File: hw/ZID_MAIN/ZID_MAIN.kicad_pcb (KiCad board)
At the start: 6 copper layers, 127 x 88.9 mm, 181 parts, among them J1 Conn 1x04 0.1" Socket, J10 FFC/FPC-40 Socket, J11 JST-PH-K B6B, J14 USB-C PWR ONLY, J15 Conn 2x03 pin hdr 0.1", J2 JST-PH-K B6B, J3 Conn 1x02 0.1" pin, J4 Conn 1x03 0.1" pin, J5 Conn 1x08 0.1" pin, J6 Conn 1x08 0.1" pin, J7 Conn 2x04 0.1" pin, J8 Conn 2x02 0.1" pin, J9 Conn 2x04 0.1" pin, M1 WS-RP2040-Zero, SW1 SW_Push, SW2 SW_DIP_x02, U1 OSC-20MHz, U10 27WZ06, U11 74LVC125AS, U12 74LVC273, U13 74FCT2245, U14 AS7C1024B, U15 ATF1508AS, U16 74FCT2245, U17 74HCT166, U18 ATF1508AS, U19 74HCT166, U2 74FCT2245, U20 74FCT2244, U22 ATF1504AS-44T, U23 74AHCT00, U24 74FCT2244, U3 24LC32, U4 MIC2775, U5 SST39SF010, U6 74LVC245, U7 74FCT2245, U8 74AHCT14, U9 Z80 C20MHz-PLCC

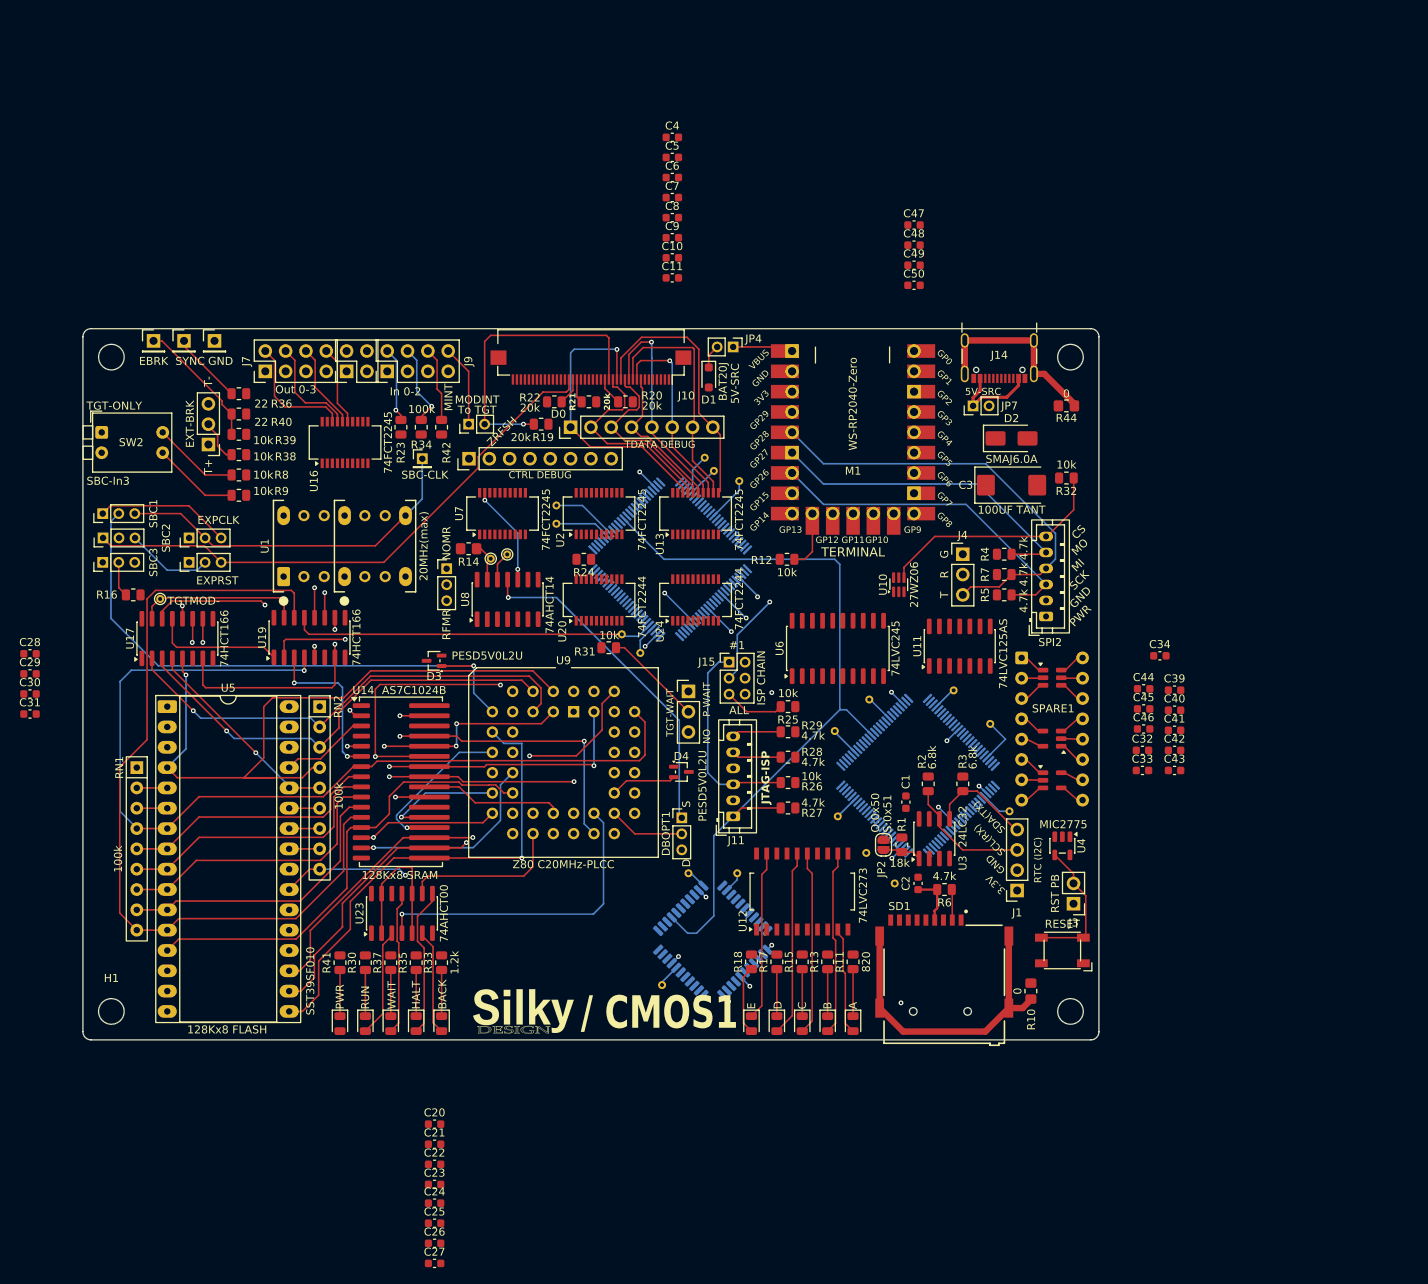
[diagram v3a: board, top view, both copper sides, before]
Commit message: PCB: Save before 'rip-out' (3.5x5.0)
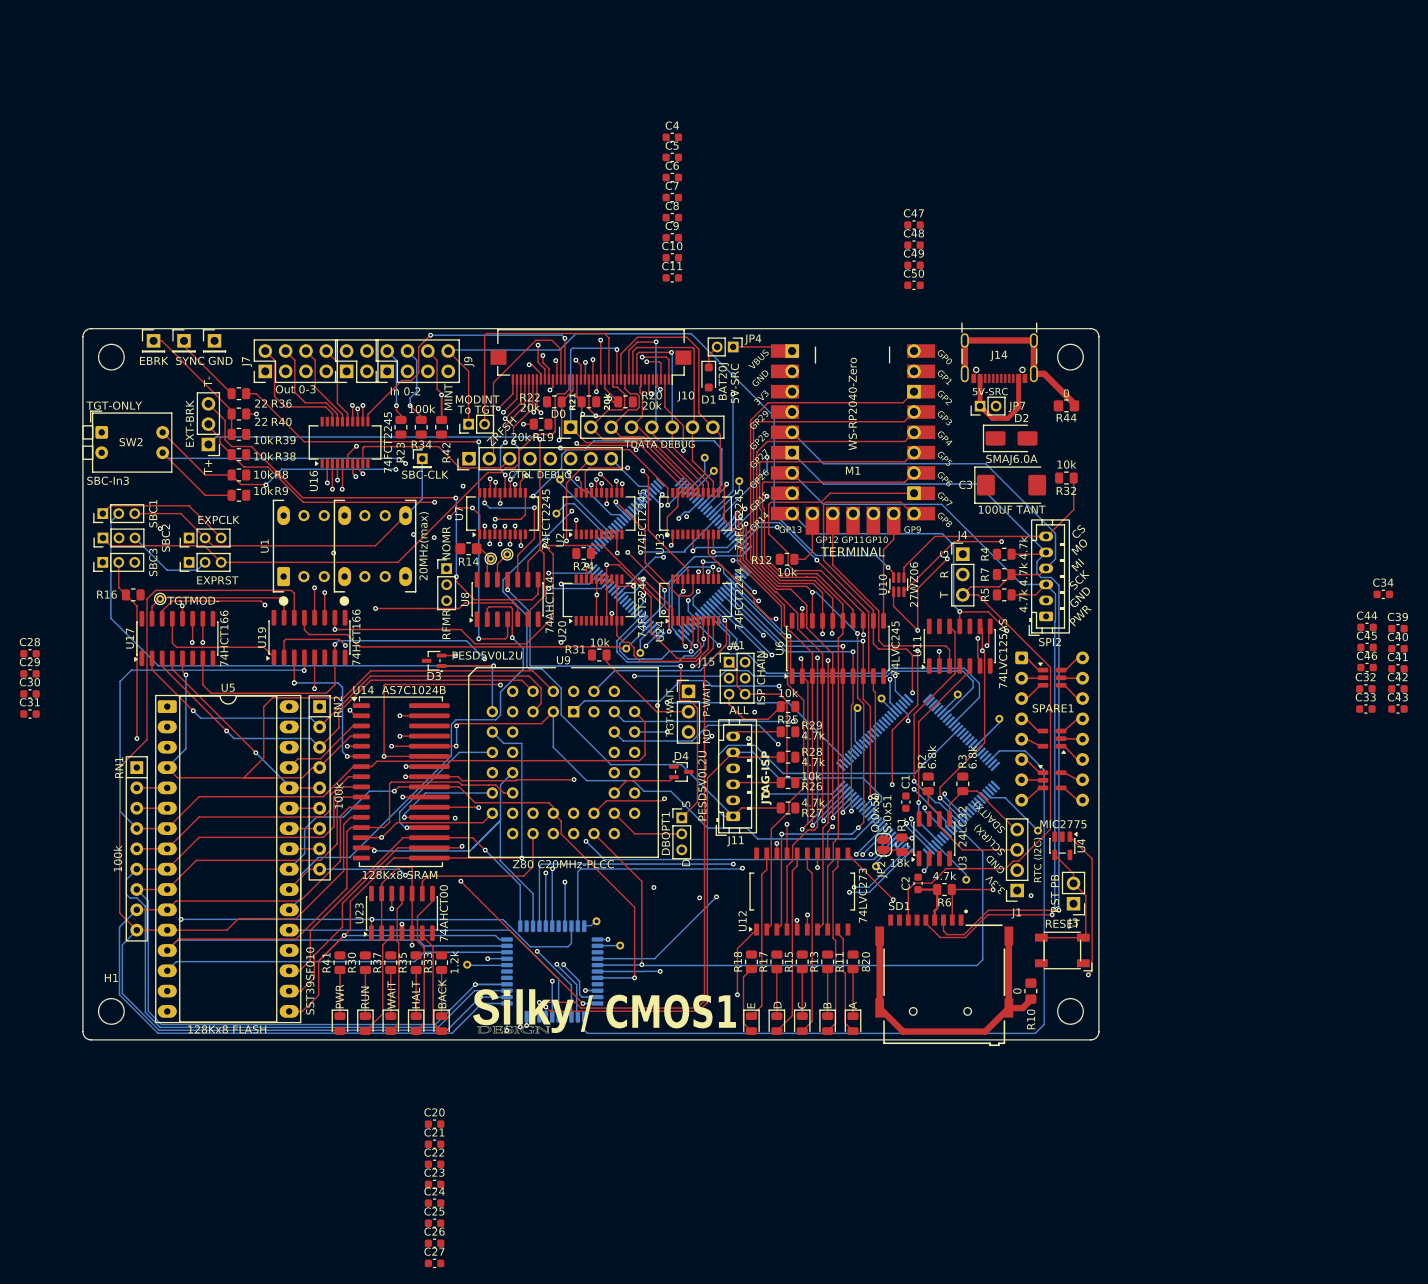
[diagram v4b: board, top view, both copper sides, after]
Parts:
- moved C32 29.0 mm to (219.1, 100.9)
- moved C33 29.0 mm to (219.1, 103.4)
- moved C34 29.0 mm to (221.3, 89.1)
- moved C39 29.0 mm to (223.1, 93.4)
- moved C40 29.0 mm to (223.1, 95.9)
- moved C41 29.0 mm to (223.1, 98.4)
- moved C42 29.0 mm to (223.1, 100.9)
- moved C43 29.0 mm to (223.1, 103.4)
- moved C44 29.0 mm to (219.3, 93.2)
- moved C45 29.0 mm to (219.3, 95.7)
- moved C46 29.0 mm to (219.3, 98.2)
- moved TP22 24.5 mm to (106.8, 135.4), turned to 180 degrees
- moved TP19 22.4 mm to (155.6, 103.3)
- moved TP18 20.5 mm to (178.1, 118.6)
- moved U22 20.5 mm to (117.4, 136.2), turned to 90 degrees
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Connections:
- U2 pad 11: /TA0 -> /TA2
- U2 pad 13: /TA2 -> /TA0
- U2 pad 14: /TA3 -> /TA15
- U2 pad 15: /TA4 -> /TA14
- U2 pad 16: /TA5 -> /TA13
- U2 pad 17: /TA6 -> /TA12
- U2 pad 18: /TA7 -> /TA11
- U2 pad 2: /ZA7 -> /ZA11
- U2 pad 3: /ZA6 -> /ZA12
- U2 pad 4: /ZA5 -> /ZA13
- U2 pad 5: /ZA4 -> /ZA14
- U2 pad 6: /ZA3 -> /ZA15
- U2 pad 7: /ZA2 -> /ZA0
- U2 pad 9: /ZA0 -> /ZA2
- U7 pad 11: /TA8 -> /TA3
- U7 pad 12: /TA9 -> /TA4
- U7 pad 13: /TA10 -> /TA5
- U7 pad 14: /TA11 -> /TA6
- U7 pad 15: /TA12 -> /TA7
- U7 pad 16: /TA13 -> /TA8
- U7 pad 17: /TA14 -> /TA9
- U7 pad 18: /TA15 -> /TA10
- U7 pad 2: /ZA15 -> /ZA10
- U7 pad 3: /ZA14 -> /ZA9
- U7 pad 4: /ZA13 -> /ZA8
- U7 pad 5: /ZA12 -> /ZA7
- U7 pad 6: /ZA11 -> /ZA6
- U7 pad 7: /ZA10 -> /ZA5
- U7 pad 8: /ZA9 -> /ZA4
- U7 pad 9: /ZA8 -> /ZA3
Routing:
- net /ZRD-: track 17.3 -> 233.7 mm, vias 0 -> 6
- net /ZWR-: track 49.7 -> 264.3 mm, vias 2 -> 7
- net /RST-: track 10.8 -> 211.3 mm, vias 0 -> 1
- net /TGTMODE-: track 20.9 -> 220.7 mm, vias 0 -> 4
- net /LRST-: track 19.0 -> 203.6 mm, vias 0 -> 4
- net /ZA0: track 103.1 -> 269.1 mm, vias 0 -> 2
- net /ZD1: track 57.7 -> 221.8 mm, vias 1 -> 3
- net /ZA3: track 160.1 -> 313.1 mm, vias 1 -> 6
- net /ZD0: track 57.9 -> 210.8 mm, vias 0 -> 3
- net /ZM1-: track 0.00 -> 136.5 mm, vias 0 -> 1
- net /TWAIT-: track 3.04 -> 134.7 mm, vias 0 -> 3
- net /ZBACK-: track 39.9 -> 165.6 mm, vias 1 -> 8
- net /MRST-: track 0.00 -> 119.3 mm, vias 0 -> 3
- net /ZRFSH-: track 8.27 -> 121.6 mm, vias 0 -> 1
- net /ZD6: track 43.8 -> 152.2 mm, vias 1 -> 5
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
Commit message: PCB: Checkpoint... 349 nets left
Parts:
- added U21: 74LVC2G34, Package_TO_SOT_SMD:SOT-23-6, F.Cu at (163.9, 82.5)
- R12, R16, R24, R31, R38, R39, R8, R9: value 10k -> 20k
- U10: value 27WZ06 -> 74LVC2G06
- U11: value 74LVC125AS -> 74LVC2G34; footprint Package_SO:SOIC-14_3.9x8.7mm_P1.27mm -> Package_TO_SOT_SMD:SOT-23-6
- U3: value 24LC32 -> 24LC32A EEP
- moved SPARE1 92.8 mm to (87.9, 126.0), turned to 90 degrees
- moved TP10 62.3 mm to (179.4, 87.1)
- moved TP11 60.0 mm to (177.4, 87.0)
- moved TP5 56.6 mm to (183.5, 103.6)
- moved TP4 56.4 mm to (183.5, 106.4)
- moved TP2 51.9 mm to (179.5, 109.5)
- moved TP18 43.2 mm to (138.6, 136.0), turned to -135 degrees
- moved TP19 42.9 mm to (119.8, 127.1), turned to -135 degrees
- moved U18 42.0 mm to (171.3, 100.1), turned to 45 degrees
- moved TP25 41.2 mm to (122.7, 122.4), turned to -135 degrees
- moved TP21 40.6 mm to (138.7, 126.0), turned to -135 degrees
- moved U15 40.2 mm to (128.6, 132.3)
- moved TP17 39.9 mm to (123.4, 143.2), turned to -135 degrees
- moved TP24 39.6 mm to (133.9, 121.6), turned to -135 degrees
- moved TP6 39.4 mm to (133.9, 142.5), turned to -135 degrees
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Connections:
- U11 pad 1: GND -> /ZRD-
- U11 pad 2: /MOD_SEL- -> GND
- U11 pad 3: /MSEL- -> /ZA0
- U11 pad 4: GND -> /MA0
- U11 pad 5: /ZA0 -> +3.3V
- U11 pad 6: /MA0 -> /MRD-
- U12 pad 12: Net-(LED2-A) -> Net-(LED4-A)
- U12 pad 16: Net-(LED4-A) -> Net-(LED2-A)
- U12 pad 19: Net-(LED5-K) -> Net-(LED1-A)
- U12 pad 9: Net-(LED1-A) -> Net-(LED5-K)
- U2 pad 11: /TA2 -> /TA11
- U2 pad 12: /TA1 -> /TA12
- U2 pad 13: /TA0 -> /TA13
- U2 pad 14: /TA15 -> /TA14
- U2 pad 15: /TA14 -> /TA15
- U2 pad 16: /TA13 -> /TA0
- U2 pad 17: /TA12 -> /TA1
- U2 pad 18: /TA11 -> /TA2
- U2 pad 2: /ZA11 -> /ZA2
- U2 pad 3: /ZA12 -> /ZA1
- U2 pad 4: /ZA13 -> /ZA0
- U2 pad 5: /ZA14 -> /ZA15
- U2 pad 6: /ZA15 -> /ZA14
- U2 pad 7: /ZA0 -> /ZA13
- U2 pad 8: /ZA1 -> /ZA12
- U2 pad 9: /ZA2 -> /ZA11
- U6 pad 1: /ZRD- -> /MRD-
- U6 pad 19: /MOD_SEL- -> /MSEL-
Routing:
- net /ZA3: track 313.1 -> 180.4 mm, vias 6 -> 7
- net /ZWR-: track 264.3 -> 136.1 mm, vias 7 -> 5
- net /SBCMODE-: track 23.0 -> 140.3 mm, vias 1 -> 2
- net /RRA1: track 34.4 -> 150.6 mm, vias 1 -> 2
- net /ZD5: track 105.4 -> 211.9 mm, vias 3 -> 9
- net /ZNMI-: track 0.00 -> 96.2 mm, vias 0 -> 1
- net /EXTBRKRQ-: track 72.9 -> 168.2 mm, vias 3 -> 2
- net /RFMR-: track 0.00 -> 94.6 mm, vias 0 -> 2
- net /ZD7: track 133.5 -> 227.2 mm, vias 4 -> 9
- net /ZA10: track 235.3 -> 141.8 mm, vias 5 -> 3
- net /SYNC: track 0.00 -> 93.0 mm, vias 0 -> 2
- net /RRA0: track 11.2 -> 101.2 mm, vias 0 -> 1
- net /ZD0: track 210.8 -> 122.4 mm
- net /ZINT-: track 0.00 -> 88.0 mm, vias 0 -> 2
- net /ZM1-: track 136.5 -> 53.0 mm
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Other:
- board size 127 x 88.9 mm -> 127 x 101.6 mm

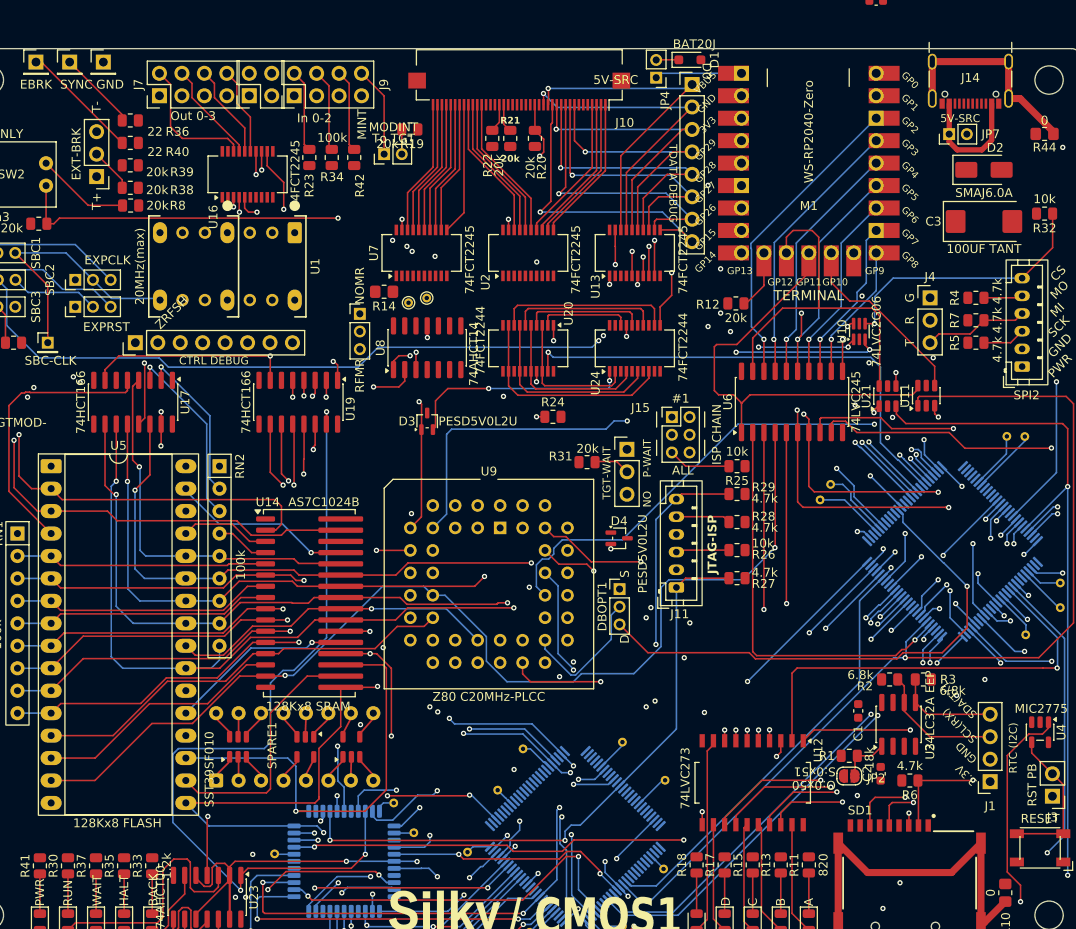
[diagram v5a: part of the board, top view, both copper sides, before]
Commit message: Checkpoint before removing JTAG-ISP Chain header (J15)
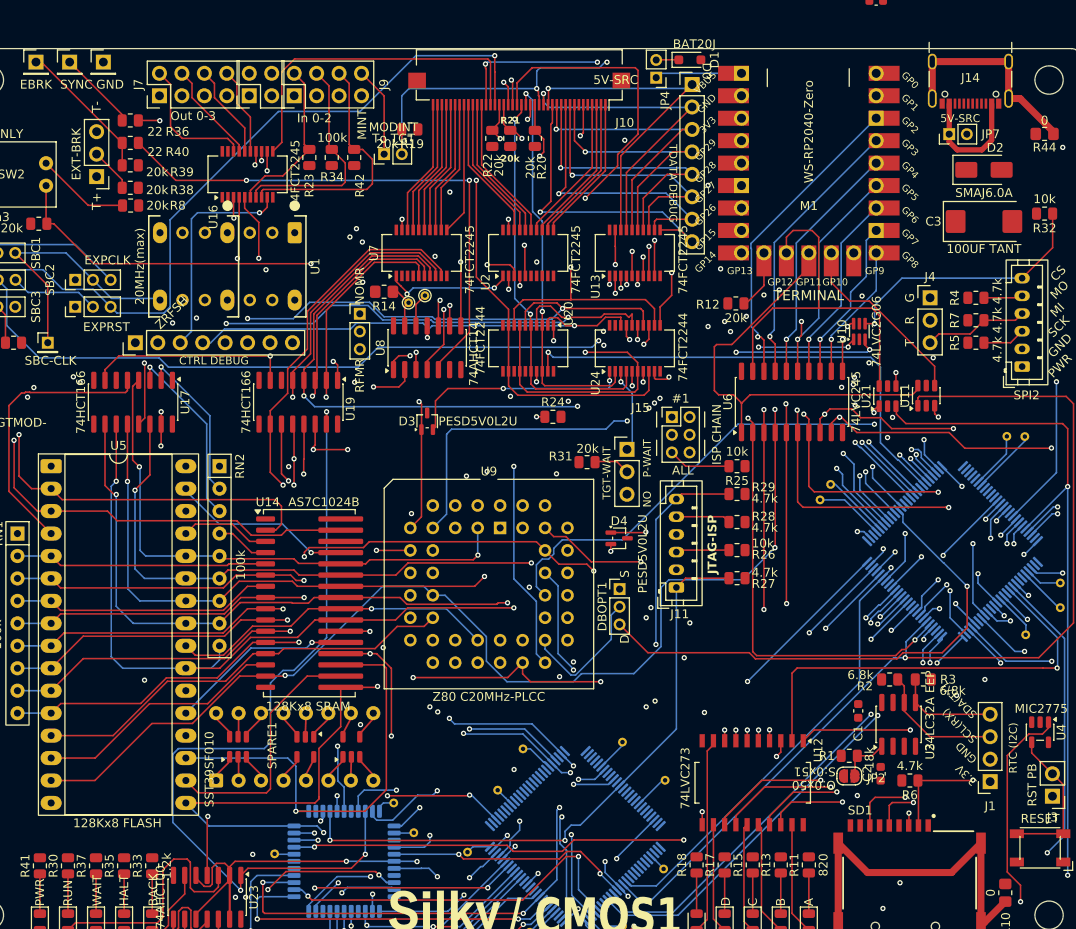
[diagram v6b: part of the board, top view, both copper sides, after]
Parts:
- moved TP7 0.35 mm to (111.6, 71.1)
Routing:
- net /TRST-: track 17.0 -> 162.7 mm, vias 0 -> 2
- net /ZRFSH-: track 59.3 -> 185.4 mm, vias 2 -> 5
- net /ZM1-: track 53.0 -> 173.9 mm, vias 1 -> 3
- net /ZWR-: track 136.1 -> 238.6 mm, vias 5 -> 8
- net /ZRD-: track 226.3 -> 311.9 mm, vias 4 -> 7
- net /ZHALT-: track 62.6 -> 134.4 mm, vias 1 -> 3
- net /ZA5: track 187.2 -> 258.3 mm, vias 4 -> 5
- net /ZA15: track 122.8 -> 192.7 mm, vias 4 -> 5
- net /TINT-: track 2.79 -> 72.2 mm, vias 0 -> 3
- net /ZA2: track 195.0 -> 262.8 mm, vias 6 -> 8
- net Net-(OP3-B): track 0.00 -> 65.8 mm, vias 0 -> 1
- net Net-(R36-Pad2): track 0.00 -> 65.3 mm, vias 0 -> 3
- net /ZA4: track 184.6 -> 249.7 mm, vias 5 -> 7
- net /ZWAIT-: track 78.4 -> 141.8 mm, vias 1 -> 3
- net Net-(R40-Pad2): track 0.00 -> 62.1 mm, vias 0 -> 2
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
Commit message: Checkpoint after removing JTAG-ISP Chain header (J15)
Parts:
- removed J15: Conn 2x03 pin hdr 0.1", Connector_PinHeader_2.00mm:PinHeader_2x03_P2.00mm_Vertical
- removed R25: 10k, Resistor_SMD:R_0805_2012Metric
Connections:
- U15 pad 4: /D2_IN -> /JTD1O2I
- U22 pad 32: /JTD3OCI -> /JTDO_CI
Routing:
- net /D2_IN: track 80.4 -> 0.00 mm, vias 2 -> 0
- net /JTD3OCI: track 80.2 -> 0.00 mm, vias 3 -> 0
- net /JTD1O2I: track 54.4 -> 0.00 mm, vias 1 -> 0
- net /JTDO_CI: track 23.4 -> 5.72 mm
- net Net-(R40-Pad2): track 62.1 -> 61.4 mm

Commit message: Checkpoint - Routing PWR/GND
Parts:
- removed TP2: TestPoint, TestPoint:TestPoint_THTPad_D1.0mm_Drill0.5mm
- moved C49 94.2 mm to (157.0, 129.3), turned to 180 degrees
- moved C50 89.9 mm to (170.8, 127.3)
- moved C48 51.1 mm to (145.1, 80.8), turned to 90 degrees
- moved C47 35.4 mm to (168.6, 65.1), turned to -90 degrees
- moved R32 3.54 mm to (181.8, 65.4)
- moved TP7 1.60 mm to (111.9, 72.7)
- moved TP3 0.74 mm to (109.8, 72.7)
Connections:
- U18 pad 88: /IOE1 -> unconnected-(U18-IN/OE1-Pad88)
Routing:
- net +3.3V: track 0.00 -> 106.3 mm, vias 0 -> 15
- net +5V: track 0.00 -> 99.8 mm, vias 0 -> 12
- net /JTD1O2I: track 0.00 -> 94.2 mm, vias 0 -> 2
- net /ZD0: track 153.8 -> 235.9 mm, vias 6 -> 7
- net /JTDO_CI: track 5.72 -> 63.3 mm, vias 0 -> 2
- net /ZA3: track 214.6 -> 266.8 mm
- net /ZD1: track 205.9 -> 254.4 mm, vias 9 -> 10
- net /JTMS: track 70.8 -> 117.4 mm, vias 2 -> 4
- net /ZA0: track 235.4 -> 279.9 mm
- net /ZIORQ-: track 137.3 -> 181.1 mm, vias 4 -> 6
- net /ZA11: track 116.5 -> 158.1 mm, vias 3 -> 5
- net /ZA8: track 102.3 -> 141.7 mm, vias 3 -> 5
- net /ZA9: track 120.5 -> 159.4 mm, vias 3 -> 6
- net /ZMREQ-: track 104.9 -> 142.0 mm, vias 2 -> 3
- net /ZA14: track 152.2 -> 185.7 mm, vias 4 -> 6
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- added copper zone on In3.Cu, net +3.3V
- added copper zone on In3.Cu, net +5V
- added copper zone on In2.Cu, net GND
